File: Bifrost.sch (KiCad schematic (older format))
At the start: 34 parts, among them J1 OIP, U1 AD5932, U3 AD8038ARZ, X1 SPXO-50M

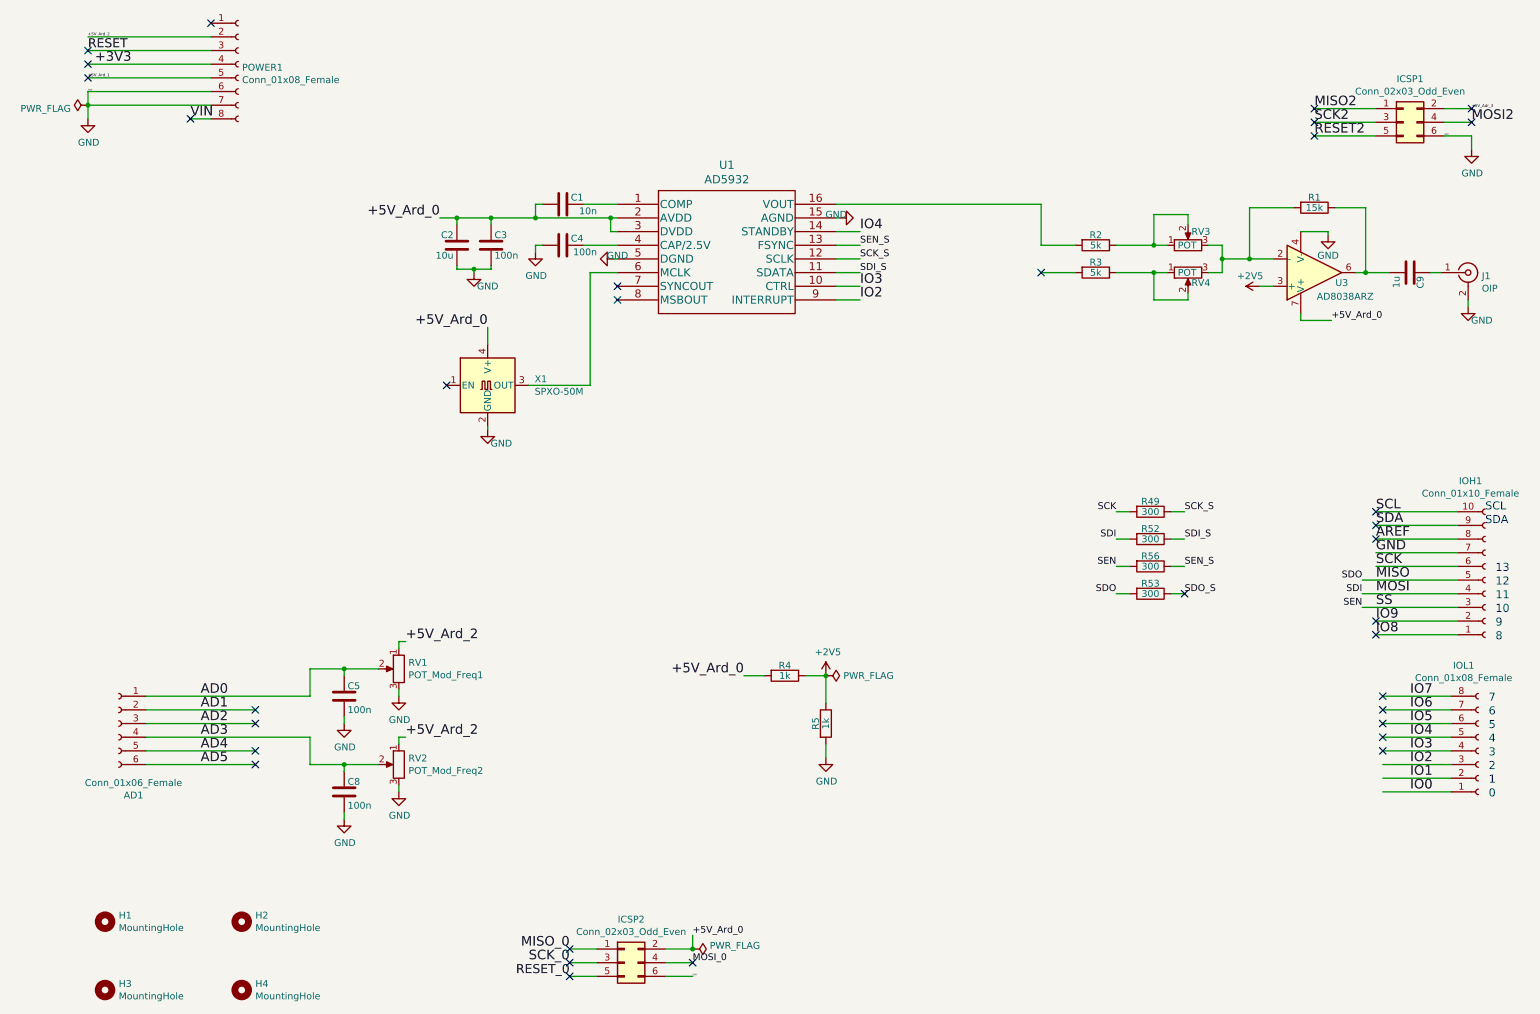
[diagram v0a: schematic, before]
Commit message: added a second ad5932
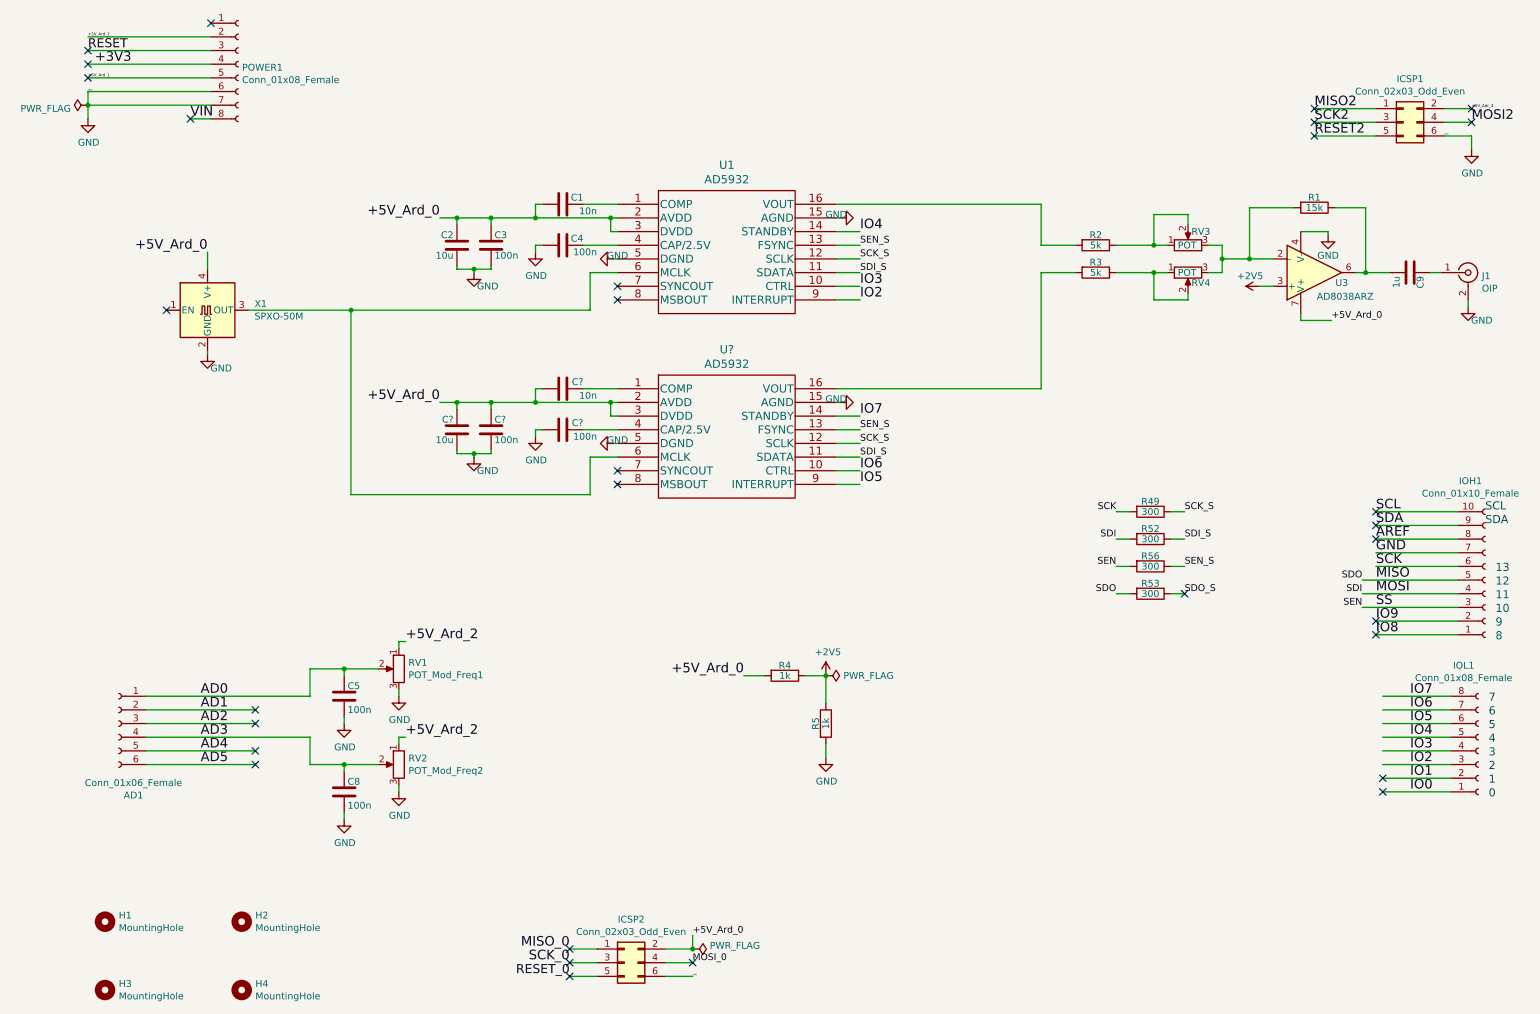
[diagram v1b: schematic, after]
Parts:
- added C? (x2): 100n, Capacitor_SMD:C_0603_1608Metric_Pad1.08x0.95mm_HandSolder, symbol Device:C
- added C?: 10u, Capacitor_SMD:C_0603_1608Metric_Pad1.08x0.95mm_HandSolder, symbol Device:C
- added C?: 10n, Capacitor_SMD:C_0603_1608Metric_Pad1.08x0.95mm_HandSolder, symbol Device:C
- added U?: AD5932, Package_SO:TSSOP-16_4.4x5mm_P0.65mm, symbol LibPersoNadj:AD5932
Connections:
- wire segments 141 -> 176
- no-connect marks 33 -> 31
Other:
- moved on the sheet: X1

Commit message: Made a AVDD and DVDD Put an offset on the output off the signal generator
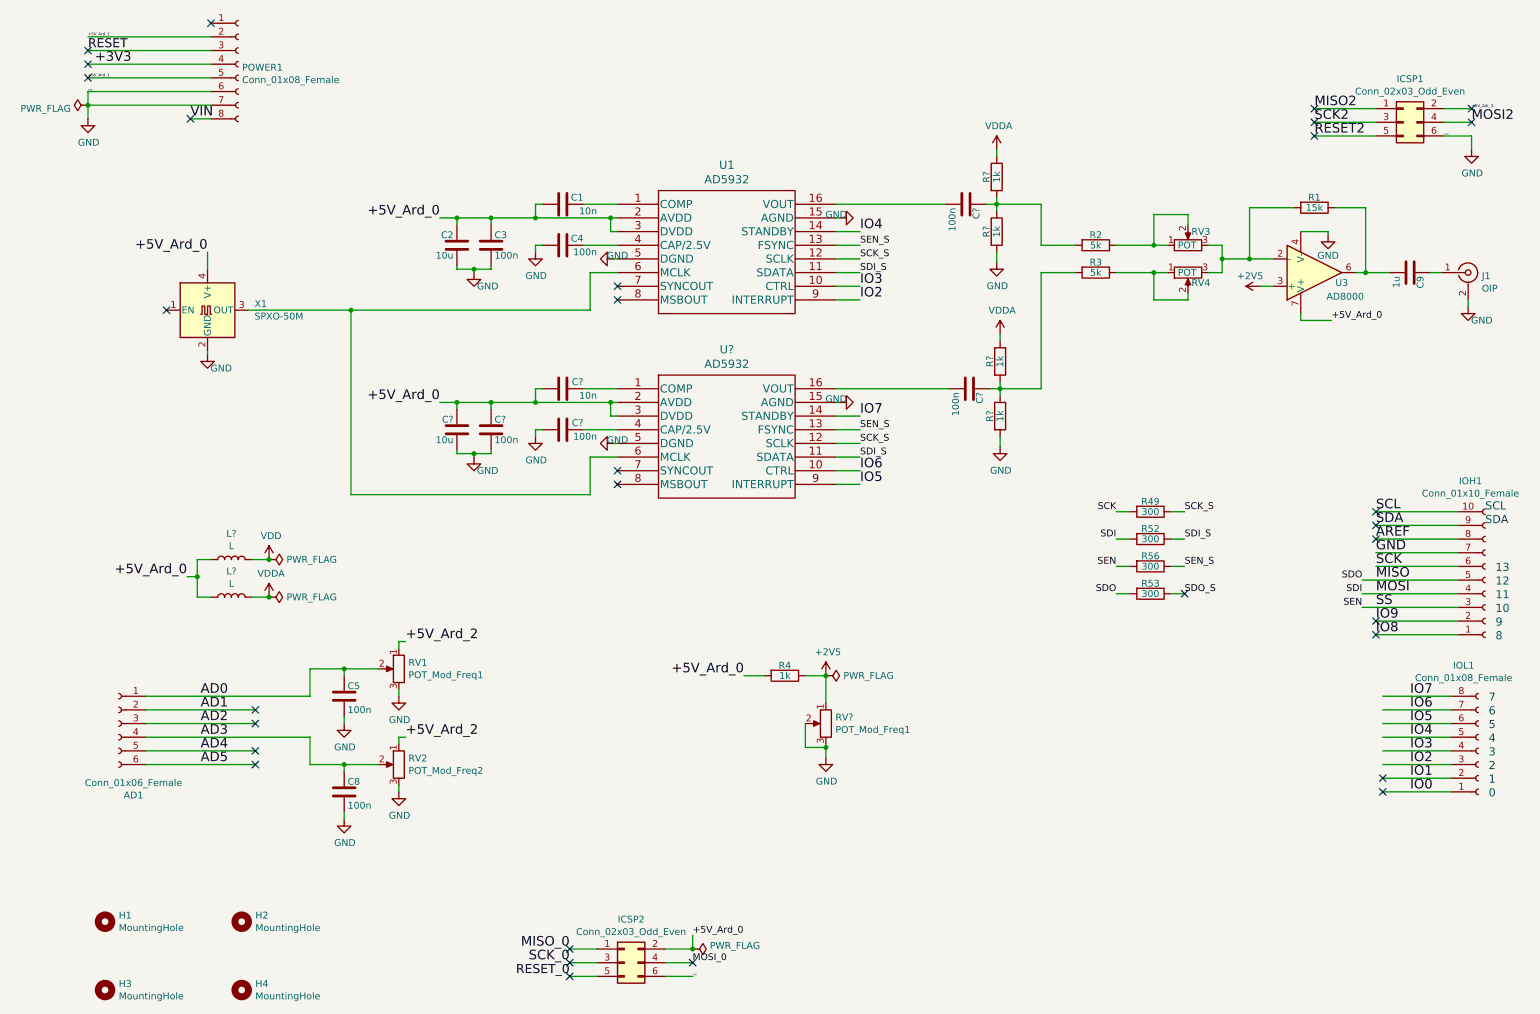
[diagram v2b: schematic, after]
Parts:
- removed R5: 1k, Resistor_SMD:R_0603_1608Metric_Pad0.98x0.95mm_HandSolder, symbol Device:R
- added C? (x2): 100n, Capacitor_SMD:C_0603_1608Metric_Pad1.08x0.95mm_HandSolder, symbol Device:C
- added L? (x2): L, symbol Device:L
- added R? (x4): 1k, Resistor_SMD:R_0603_1608Metric_Pad0.98x0.95mm_HandSolder, symbol Device:R
- added RV?: POT_Mod_Freq1, Potentiometer_THT:Potentiometer_Bourns_3266Y_Vertical, symbol Device:R_POT
- U3: value AD8038ARZ -> AD8000
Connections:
- net labels added: VDD, VDDA
- wire segments 176 -> 198

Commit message: Added fixed gain amplifiers Tweaked the filtering of AVDD & DVDD Began placing componants Put in feuille hierarchique
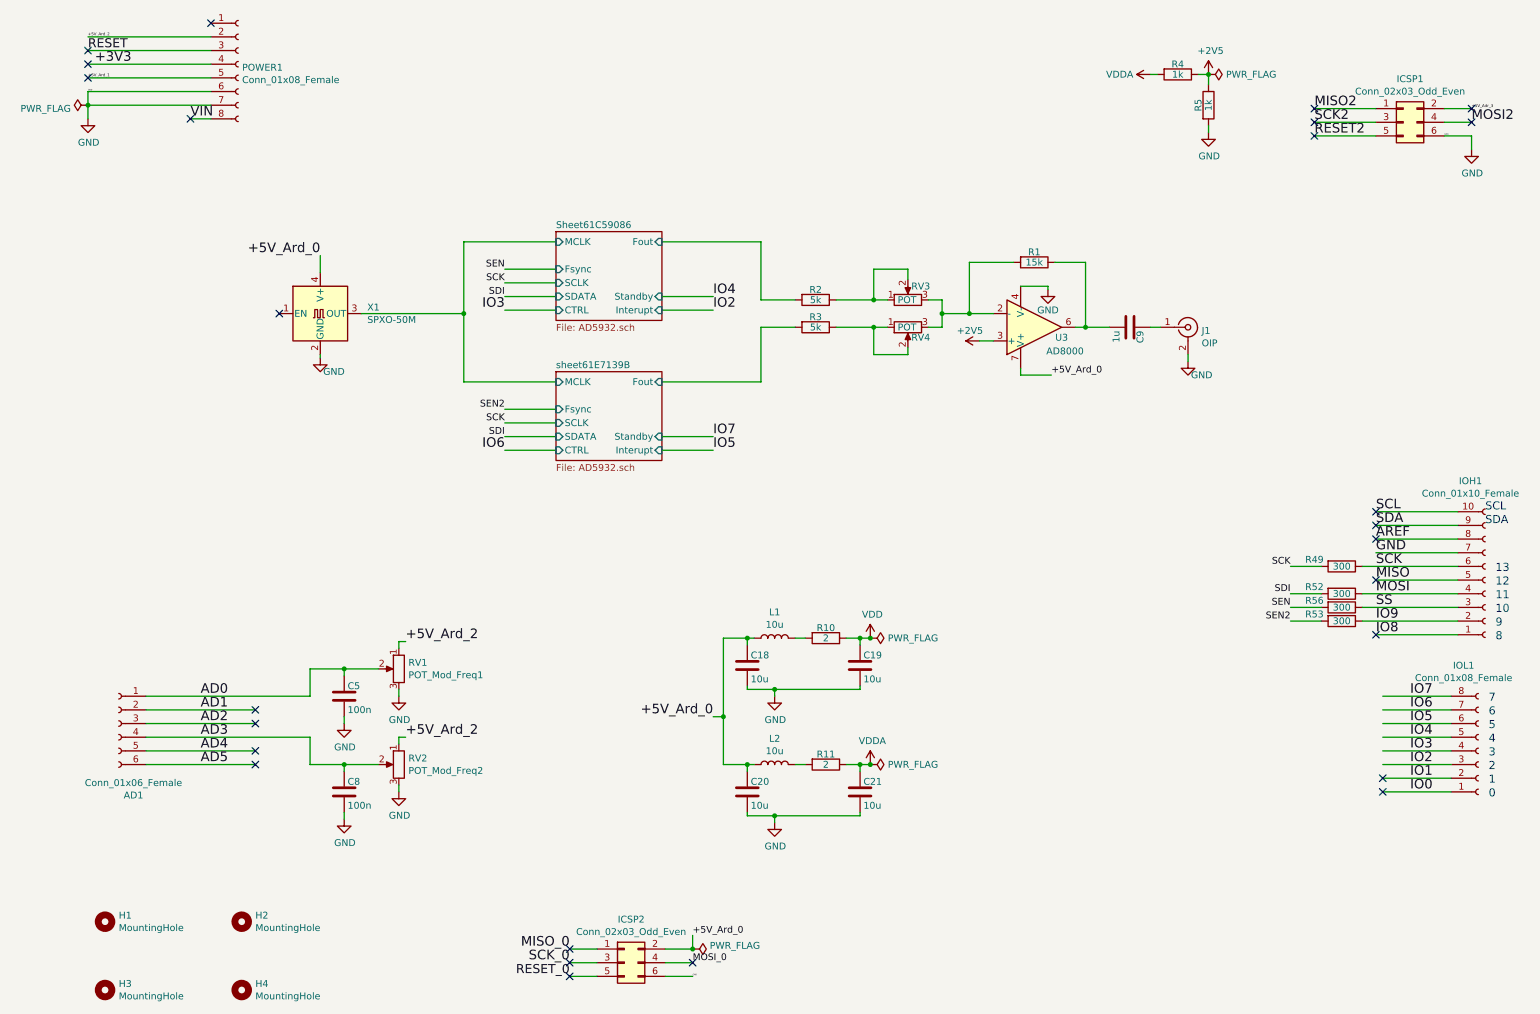
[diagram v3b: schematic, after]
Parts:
- removed C1, C?: 10n, Capacitor_SMD:C_0603_1608Metric_Pad1.08x0.95mm_HandSolder, symbol Device:C
- removed C2, C?: 10u, Capacitor_SMD:C_0603_1608Metric_Pad1.08x0.95mm_HandSolder, symbol Device:C
- removed C3, C4, C? (x4): 100n, Capacitor_SMD:C_0603_1608Metric_Pad1.08x0.95mm_HandSolder, symbol Device:C
- removed R? (x4): 1k, Resistor_SMD:R_0603_1608Metric_Pad0.98x0.95mm_HandSolder, symbol Device:R
- removed RV?: POT_Mod_Freq1, Potentiometer_THT:Potentiometer_Bourns_3266Y_Vertical, symbol Device:R_POT
- removed U1, U?: AD5932, Package_SO:TSSOP-16_4.4x5mm_P0.65mm, symbol LibPersoNadj:AD5932
- added C18, C19, C20, C21: 10u, Capacitor_SMD:C_0603_1608Metric_Pad1.08x0.95mm_HandSolder, symbol Device:C
- added R10, R11: 2, Resistor_SMD:R_0603_1608Metric_Pad0.98x0.95mm_HandSolder, symbol Device:R
- added R5: 1k, Resistor_SMD:R_0603_1608Metric_Pad0.98x0.95mm_HandSolder, symbol Device:R
- L1, L2: renamed from L?; value L -> 10u; footprint (none) -> Inductor_SMD:L_0603_1608Metric_Pad1.05x0.95mm_HandSolder
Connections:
- net labels added: SEN2
- net labels removed: SCK_S, SDI_S, SDO, SDO_S, SEN_S
- wire segments 198 -> 152
- no-connect marks 31 -> 26
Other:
- moved on the sheet: C9, J1, L1, L2, R1, R2, R3, R4, R49, R52, R53, R56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

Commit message: Implemented the LMH6881 instead of the AD8000 Continued routing
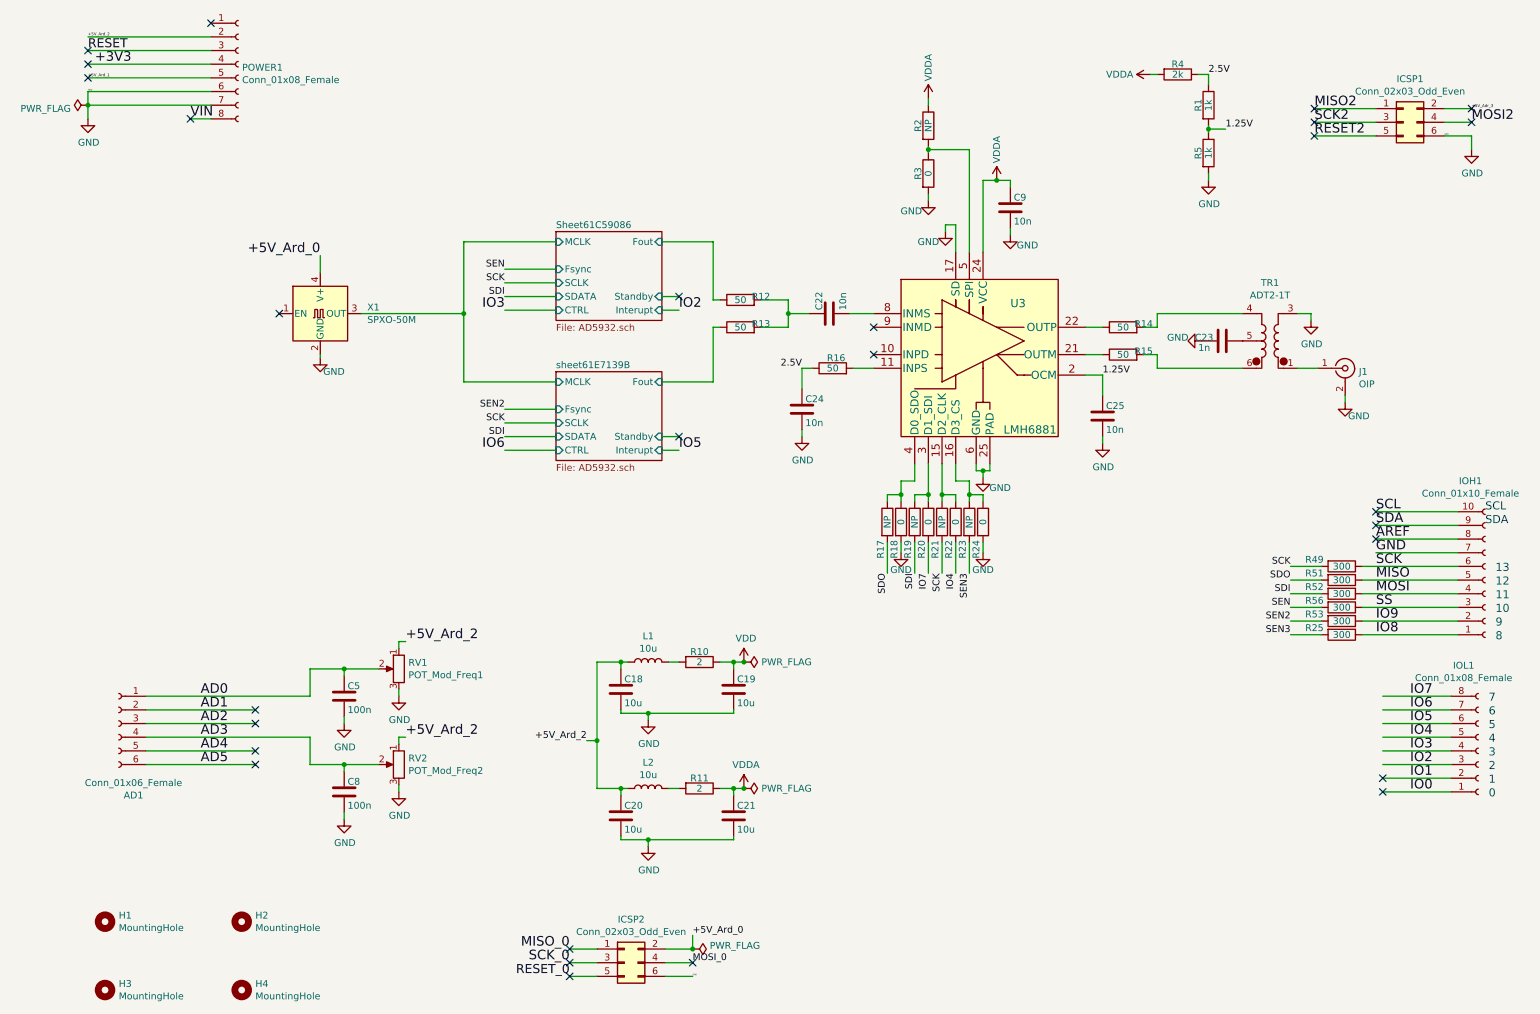
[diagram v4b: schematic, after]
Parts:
- removed RV3, RV4: POT, Potentiometer_THT:Potentiometer_Bourns_3266Y_Vertical, symbol Device:R_POT
- removed U3: AD8000, Package_SO:SOIC-8_3.9x4.9mm_P1.27mm, symbol Amplifier_Operational:AD8001AR
- added C22, C24, C25: 10n, Capacitor_SMD:C_0603_1608Metric_Pad1.08x0.95mm_HandSolder, symbol Device:C
- added C23: 1n, Capacitor_SMD:C_0603_1608Metric_Pad1.08x0.95mm_HandSolder, symbol Device:C
- added R12, R13, R14, R15, R16: 50, Resistor_SMD:R_0603_1608Metric_Pad0.98x0.95mm_HandSolder, symbol Device:R
- added R17, R19, R21, R23: NP, Resistor_SMD:R_0603_1608Metric_Pad0.98x0.95mm_HandSolder, symbol Device:R
- added R18, R20, R22, R24: 0, Resistor_SMD:R_0603_1608Metric_Pad0.98x0.95mm_HandSolder, symbol Device:R
- added R25, R51: 300, Resistor_SMD:R_0603_1608Metric_Pad0.98x0.95mm_HandSolder, symbol Device:R
- added TR1: ADT2-1T, RF_Mini-Circuits:Mini-Circuits_CD542_H2.84mm, symbol LibPersoNadj:ADT2-1T
- added U3: LMH6881, Package_DFN_QFN:WQFN-24-1EP_4x4mm_P0.5mm_EP2.45x2.45mm, symbol LibPersoNadj:LMH6881
- C9: value 1u -> 10n
- R1: value 15k -> 1k
- R2: value 5k -> NP
- R3: value 5k -> 0
- R4: value 1k -> 2k
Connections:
- net labels added: 1.25V, 2.5V, SDO, SEN3
- net labels removed: +2V5
- wire segments 152 -> 200
- no-connect marks 26 -> 28
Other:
- moved on the sheet: C18, C19, C20, C21, J1, L1, L2, R10, R11, R5
